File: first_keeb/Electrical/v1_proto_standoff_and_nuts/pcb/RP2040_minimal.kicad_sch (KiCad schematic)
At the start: 62 parts, among them P1 USB-TYPE-C-016, Q1 SN74LV1T34DBV, SW1 SKRKAHE020, SW2 BUTT0, SW3 BUTT1, U1 NCP1117-3.3_SOT223, U2 MCP1525-TT, U3 PRTR5V0U2X, U4 MCP6004, U5 STM32F401RCTx, Y1 16MHz

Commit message: stm32 pcb almost done
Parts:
- removed C1, C2: 10u, Capacitor_SMD:C_0805_2012Metric, symbol Device:C
- removed R10, R3, R5, R7, R8: 0, Capacitor_SMD:C_0603_1608Metric, symbol Device:R
- removed U1: NCP1117-3.3_SOT223, Package_TO_SOT_SMD:SOT-223-3_TabPin2, symbol Regulator_Linear:NCP1117-3.3_SOT223
- removed U2: MCP1525-TT, Package_TO_SOT_SMD:SOT-23, symbol Reference_Voltage:MCP1525-TT
- removed U4: MCP6004, Package_SO:SOIC-14_3.9x8.7mm_P1.27mm, symbol Amplifier_Operational:MCP6004
- added C11, C12: 10u, Capacitor_SMD:C_1206_3216Metric, symbol Device:C
- added C13, C6: 100n, Capacitor_SMD:C_0402_1005Metric, symbol Device:C_Small
- added D1: 1N4148WS, Diode_SMD:D_SOD-323, symbol Diode:1N4148WS
- added FB1: GZ2012D601TF, Capacitor_SMD:C_0805_2012Metric, symbol Device:FerriteBead
- added J1, J2: Conn_01x04_Socket, Connector_PinSocket_2.54mm:PinSocket_1x04_P2.54mm_Vertical, symbol Connector:Conn_01x04_Socket
- added R10, R11, R6, R7: DNP, Resistor_SMD:R_0402_1005Metric, symbol Device:R_Small
- added R12, R13: 0, Resistor_SMD:R_0402_1005Metric, symbol Device:R_Small
- added R4: DNP, Capacitor_SMD:C_0603_1608Metric, symbol Device:R
- added R5: 10k, Resistor_SMD:R_0402_1005Metric, symbol Device:R_Small
- added SW2: SKRKAHE020, Button_Switch_SMD:SW_Push_SPST_NO_Alps_SKRK, symbol Switch:SW_Push
- added SW4: BUTT3, Button_Switch_SMD:SW_Push_1P1T_NO_6x6mm_H9.5mm, symbol Switch:SW_Push
- added U1: AMS1117-2.5, Package_TO_SOT_SMD:SOT-223-3_TabPin2, symbol Regulator_Linear:AMS1117-2.5
- added U2: ME6208A44M3G, Package_TO_SOT_SMD:SOT-23, symbol Regulator_Linear:ME6208A44M3G
- added U5, U6: MCP6001-OT, Package_TO_SOT_SMD:SOT-23-5, symbol Amplifier_Operational:MCP6001-OT
- C10: value 1u -> 10u; footprint Capacitor_SMD:C_0402_1005Metric -> Capacitor_SMD:C_1206_3216Metric
- C9: value 100n -> 10u; footprint Capacitor_SMD:C_0402_1005Metric -> Capacitor_SMD:C_1206_3216Metric
- R9: value 0 -> DNP; now not fitted
- SW3: renamed from SW2; value BUTT0 -> BUTT1
- SW5: renamed from SW3; value BUTT1 -> BUTT2
- renumbered C3 to C1, C13 to C14, C14 to C15, C15 to C16, C16 to C17, C17 to C18, C18 to C19, C4 to C2, C19 to C20, C20 to C21, C21 to C22, C22 to C23, C23 to C24, C24 to C25, C25 to C26, C26 to C27, C27 to C28, C28 to C29, C5 to C3, C6 to C4, C7 to C5, C11 to C7, C12 to C8, D9 to D10, D10 to D11, D1 to D2, D2 to D3, D3 to D4, D4 to D5, D5 to D6, D6 to D7, D7 to D8, D8 to D9, R6 to R3, R4 to R8, U5 to U4, U6 to U7, U7 to U9
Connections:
- net ALT_ADC_IN2 is gone; now on net ADC_IN1: U4.23 (PA7)
- net ALT_ADC_IN3 is gone; now on net ADC_IN2: U4.24 (PC4)
- net LED_D_5V is gone; now on net LED_D: Q1.2 (A)
- net +5V: now also C9.1, C11.1, D1.2 (A), U1.3 (VI), U2.3 (VI); no longer Q1.5 (VCC)
- net ADC_IN1: now also U7.3 (Vout); no longer R9.2, U4.25 (PC5)
- net ADC_IN2: now also R12.1, R7.1; no longer U4.26 (PB0)
- net ADC_IN3: now also U4.25 (PC5), R11.1, R13.1; no longer U4.27 (PB1)
- net GND: now also C9.2, C11.2, C12.2, C13.2, C6.2, J2.4 (Pin_4), R5.1, SW2.2, SW4.2, U1.1 (GND), U2.1 (GND), U5.2 (V-), U6.2 (V-); no longer C9.1
- net NRST: now also C13.1, J1.1 (Pin_1), SW2.1
- net SWCLK: now also U4.49 (PA14), J1.3 (Pin_3)
- net SWDIO: now also U4.46 (PA13), J1.2 (Pin_2)
- net SWO: now also U4.55 (PB3), J1.4 (Pin_4)
- net BUTT0: now reaches U4.15 (PA1)
- net BUTT0: now also SW3.1
- net BUTT1: now reaches U4.16 (PA2)
- net BUTT1: now also SW5.1
- net BUTT2: now reaches U4.17 (PA3)
- net BUTT2: now also SW4.1
- net BOOT1: now reaches U4.28 (PB2)
- net BOOT1: now also R5.2
- net LED_D: now reaches U4.40 (PC9)
- net USART1_TX: now reaches U4.58 (PB6)
- net USART1_TX: now also J2.3 (Pin_3)
- net USART1_RX: now reaches U4.59 (PB7)
- net USART1_RX: now also J2.2 (Pin_2)
- net +3V3 renamed VDD
- net VDD: now also C10.1, C6.1, FB1.1, J2.1 (Pin_1), U1.2 (VO); no longer C17.2, C18.2, C19.2, C9.2, U7.1 (VCC), U8.1 (VCC), U9.1 (VCC)
- net ADC_VREF renamed VDDA
- net VDDA: now also FB1.2; no longer C10.1
- net ALT_ADC_IN1: no longer names the net of U4.22 (PA6)
- net A_OUT1: no longer names the net of R9.1
- net A_OUT1: now also U6.5 (V+); no longer U7.3 (Vout)
- net A_OUT2 renamed ALT_ADC_2
- net ALT_ADC_2: now also R12.2, R6.2
- net A_OUT3 renamed ALT_ADC_3
- net ALT_ADC_3: now also R10.2, R13.2
- new net: R4.1, U5.5 (V+)
- new net: R11.2, U6.1, U6.4 (-)
- new net: R10.1, U6.3 (+)
- new net: D1.1 (K), Q1.5 (VCC)
- new net: R7.2, U5.1, U5.4 (-)
- new net: R6.1, U5.3 (+)
- new net +4V4: C12.1, C17.2, C18.2, C19.2, R4.2, R9.2, U2.2 (VO), U7.1 (VCC), U8.1 (VCC), U9.1 (VCC)
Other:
- note added: "8 MHz is QMK default"
- note added: "Do not connect more than 3 sensors because dropout voltage increases with current"
- note added: "MCU Power"
- note added: "Reccomend tantalum cap for improved stability on power supplies. To be cost effective, put the tantalum caps on MCU power first since the ADC uses that as its VREF and that requires more stability than the sensors"
- note added: "STM32 powered at 2.5V would have I/O VOH of 2.5-0.4 = 2.1V worst case. VIH of LED is 0.7*5.25 = 3.675V worst case. We want to select Vcc of the Shifter such that it is both low enough to reliably recieve the data from STM32, while also high enough to reliably send data to the LED."
- note added: "Sensor Power"
- note removed: "ADC VREF"
- note removed: "Backlight"
- note removed: "Underglow"
- moved on the sheet: C1, C14, C15, C16, C18, C2, C3, C4, C5, C7, C8, F1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

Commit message: vcc pour and ground
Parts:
- removed R10, R11, R6, R7: DNP, Resistor_SMD:R_0402_1005Metric, symbol Device:R_Small
- removed R12, R13: 0, Resistor_SMD:R_0402_1005Metric, symbol Device:R_Small
- removed R4, R9: DNP, Capacitor_SMD:C_0603_1608Metric, symbol Device:R
- added C30, C31, C32: 100n, Capacitor_SMD:C_0402_1005Metric, symbol Device:C
- added D12, D13, D14: WS2812B-2020, LED_SMD:LED_WS2812B-2020_PLCC4_2.0x2.0mm, symbol LED:WS2812B-2020
- added SW6, SW8: SW_DPDT_x2, symbol Switch:SW_DPDT_x2
- added SW7: SW_SPDT, symbol Switch:SW_SPDT
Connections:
- net +4V4: now also SW7.2 (B)
- net +5V: now also C30.1, C31.1, C32.1, D12.4 (VDD), D13.4 (VDD), D14.4 (VDD)
- net ADC_IN2: now also SW6.2 (B)
- net ADC_IN3: now also SW8.2 (B)
- net ALT_ADC_2: now also U5.3 (+), SW6.6 (C); no longer U8.3 (Vout)
- net ALT_ADC_3: now also U6.3 (+), SW8.6 (C); no longer U9.3 (Vout)
- net GND: now also C30.2, C31.2, C32.2, D12.2 (GND), D13.2 (GND), D14.2 (GND)
- net V_test: now reaches U6.5 (V+)
- net V_test: now also U5.5 (V+), SW7.3 (C)
- net O_ADC_IN3: now reaches U6.1, U6.4 (-)
- net O_ADC_IN3: now also SW8.3 (C)
- net O_ADC_IN2: now reaches U5.1, U5.4 (-)
- net O_ADC_IN2: now also SW6.3 (C)
- new net: D13.1 (DOUT), D14.3 (DIN)
- new net: D12.1 (DOUT), D13.3 (DIN)
- new net S_ADC_IN2: SW6.1 (A), SW6.5 (B), U8.3 (Vout)
- new net S_ADC_IN3: SW8.1 (A), SW8.5 (B), U9.3 (Vout)
- no-connect marks 2 -> 5
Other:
- moved on the sheet: C17, C18, C19, C24, C25, C26, C27, C28, C29, D10, D11, D6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

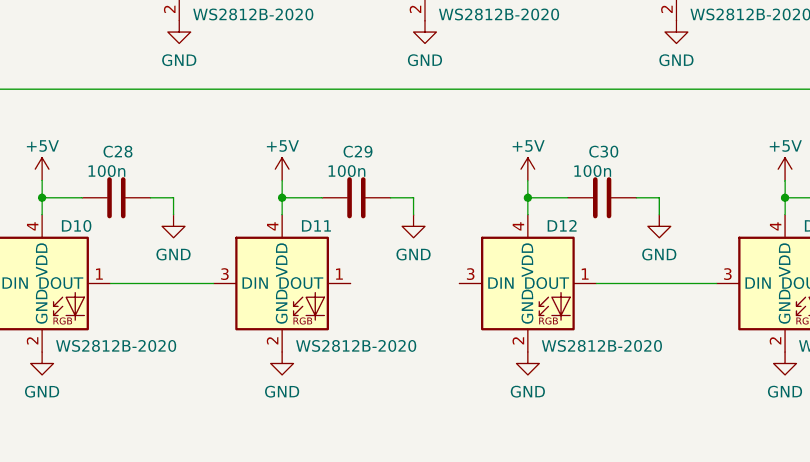
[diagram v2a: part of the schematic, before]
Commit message: adds leds
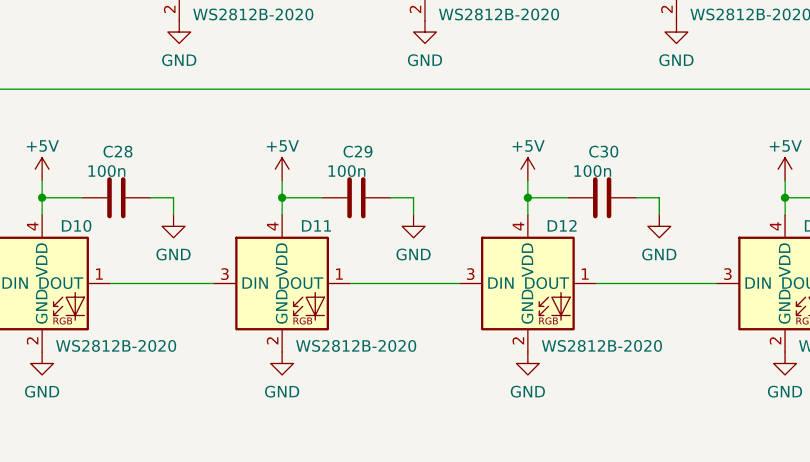
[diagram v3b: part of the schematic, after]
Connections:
- net at D12.3 (DIN): now also D11.1 (DOUT)
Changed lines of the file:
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@@
+    (stroke (width 0) (type default))
+  )
+  (wire (pts (xy 203.2 262.89) (xy 215.265 262.89))
     (stroke (width 0) (type default))
   )

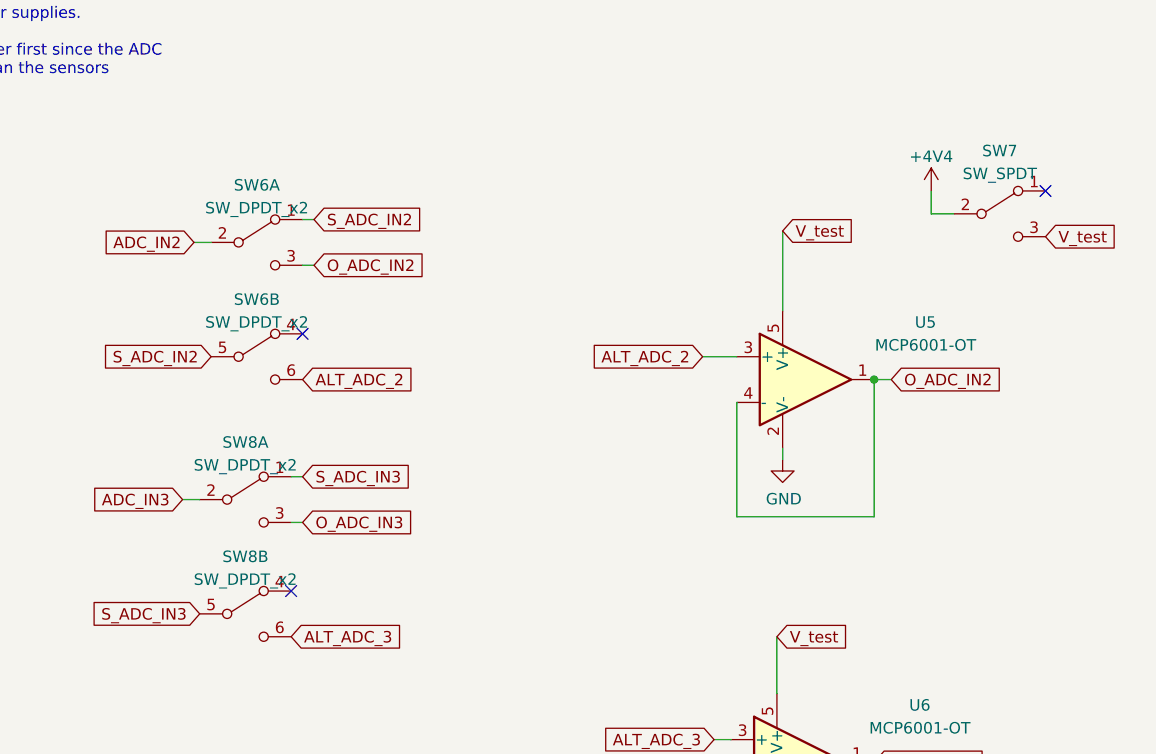
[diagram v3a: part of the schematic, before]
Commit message: finishes pcb v1 with smaller radius
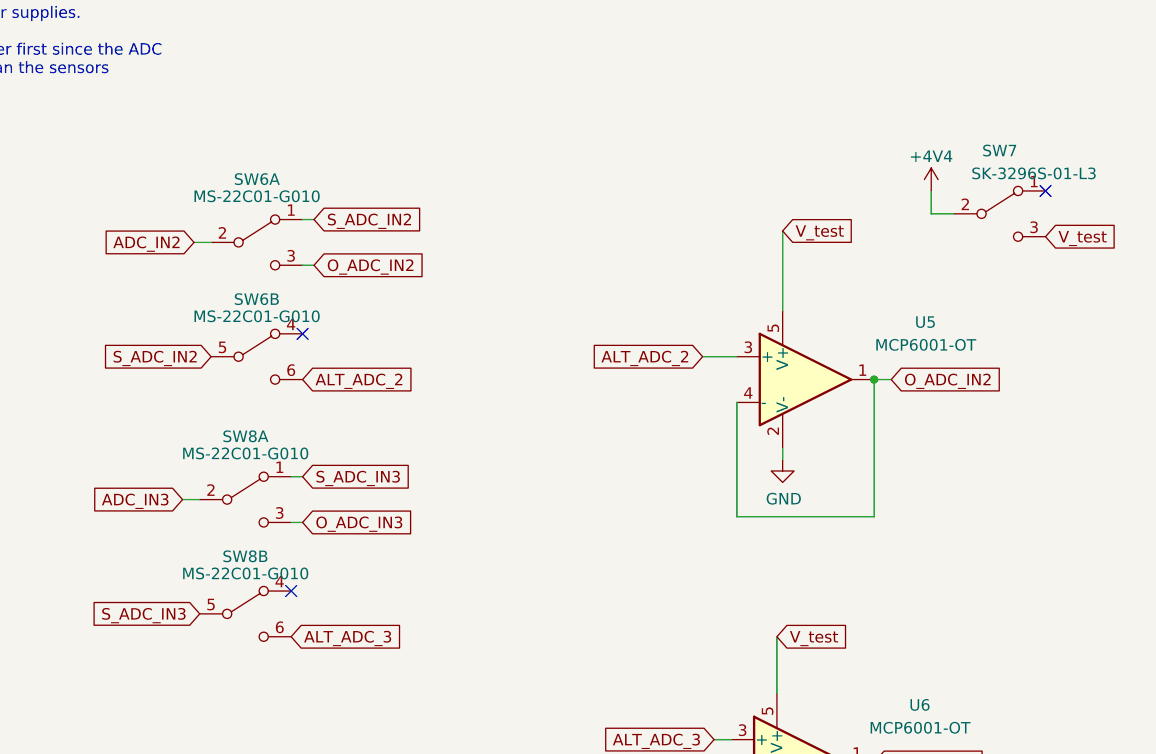
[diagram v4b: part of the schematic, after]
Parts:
- SW6, SW8: value SW_DPDT_x2 -> MS-22C01-G010; footprint (none) -> Button_Switch_SMD:DPDT-MS-22C01
- SW7: value SW_SPDT -> SK-3296S-01-L3; footprint (none) -> Button_Switch_SMD:SW_SPDT_PCM12
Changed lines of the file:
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@@
   )
   (symbol (lib_id "Switch:SW_DPDT_x2") (at 307.34 136.525 0) (unit 2)
-    (in_bom yes) (on_board yes) (dnp no) (fields_autoplaced)
+    (in_bom yes) (on_board yes) (dnp no)
     (property "Reference" "SW8" (at 307.34 130.175 0)
       (effects (font (size 1.27 1.27)))
     )
-    (property "Value" "SW_DPDT_x2" (at 307.34 132.715 0)
-      (effects (font (size 1.27 1.27)))
-    )
-    (property "Footprint" "" (at 307.34 136.525 0)
+    (property "Value" "MS-22C01-G010" (at 307.34 132.08 0)
+      (effects (font (size 1.27 1.27)))
+    )
+    (property "Footprint" "Button_Switch_SMD:DPDT-MS-22C01" (at 307.34 136.525 0)
       (effects (font (size 1.27 1.27)) hide)
     )
@@
   )
   (symbol (lib_id "Switch:SW_DPDT_x2") (at 307.34 123.825 0) (unit 1)
-    (in_bom yes) (on_board yes) (dnp no) (fields_autoplaced)
-    (property "Reference" "SW8" (at 307.34 117.475 0)
-      (effects (font (size 1.27 1.27)))
-    )
-    (property "Value" "SW_DPDT_x2" (at 307.34 120.015 0)
-      (effects (font (size 1.27 1.27)))
-    )
-    (property "Footprint" "" (at 307.34 123.825 0)
+    (in_bom yes) (on_board yes) (dnp no)
+    (property "Reference" "SW8" (at 307.34 116.84 0)
+      (effects (font (size 1.27 1.27)))
+    )
+    (property "Value" "MS-22C01-G010" (at 307.34 118.745 0)
+      (effects (font (size 1.27 1.27)))
+    )
+    (property "Footprint" "Button_Switch_SMD:DPDT-MS-22C01" (at 307.34 123.825 0)
       (effects (font (size 1.27 1.27)) hide)
     )
@@
   )
   (symbol (lib_id "Switch:SW_DPDT_x2") (at 308.61 107.95 0) (unit 2)
-    (in_bom yes) (on_board yes) (dnp no) (fields_autoplaced)
+    (in_bom yes) (on_board yes) (dnp no)
     (property "Reference" "SW6" (at 308.61 101.6 0)
       (effects (font (size 1.27 1.27)))
     )
-    (property "Value" "SW_DPDT_x2" (at 308.61 104.14 0)
-      (effects (font (size 1.27 1.27)))
-    )
-    (property "Footprint" "" (at 308.61 107.95 0)
+    (property "Value" "MS-22C01-G010" (at 308.61 103.505 0)
+      (effects (font (size 1.27 1.27)))
+    )
+    (property "Footprint" "Button_Switch_SMD:DPDT-MS-22C01" (at 308.61 107.95 0)
       (effects (font (size 1.27 1.27)) hide)
     )
@@
   )
   (symbol (lib_id "Switch:SW_SPDT") (at 391.16 92.075 0) (unit 1)
-    (in_bom yes) (on_board yes) (dnp no) (fields_autoplaced)
+    (in_bom yes) (on_board yes) (dnp no)
     (property "Reference" "SW7" (at 391.16 85.09 0)
       (effects (font (size 1.27 1.27)))
     )
-    (property "Value" "SW_SPDT" (at 391.16 87.63 0)
-      (effects (font (size 1.27 1.27)))
-    )
-    (property "Footprint" "" (at 391.16 92.075 0)
+    (property "Value" "SK-3296S-01-L3" (at 394.97 87.63 0)
+      (effects (font (size 1.27 1.27)))
+    )
+    (property "Footprint" "Button_Switch_SMD:SW_SPDT_PCM12" (at 391.16 92.075 0)
       (effects (font (size 1.27 1.27)) hide)
     )
@@
   )
   (symbol (lib_id "Switch:SW_DPDT_x2") (at 308.61 95.25 0) (unit 1)
-    (in_bom yes) (on_board yes) (dnp no) (fields_autoplaced)
-    (property "Reference" "SW6" (at 308.61 88.9 0)
-      (effects (font (size 1.27 1.27)))
-    )
-    (property "Value" "SW_DPDT_x2" (at 308.61 91.44 0)
-      (effects (font (size 1.27 1.27)))
-    )
-    (property "Footprint" "" (at 308.61 95.25 0)
-      (effects (font (size 1.27 1.27)) hide)
-    )
+    (in_bom yes) (on_board yes) (dnp no)
+    (property "Reference" "SW6" (at 308.61 88.265 0)
+      (effects (font (size 1.27 1.27)))
+    )
+    (property "Value" "MS-22C01-G010" (at 308.61 90.17 0)
+      (effects (font (size 1.27 1.27)))
+    )
+    (property "Footprint" "Button_Switch_SMD:DPDT-MS-22C01" (at 308.61 95.25 0)
+      (effects (font (size 1.27 1.27)) hide)
+    )
